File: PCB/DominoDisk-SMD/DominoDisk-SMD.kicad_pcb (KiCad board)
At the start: 2 copper layers, 45.7 x 38.9 mm, 32 parts, among them J1 Daisy port out, J2 ICSP_ISP6, J3 UART, J4 Daisy port in, K1 HYC77-TF09-200, U1 PC817C-S, U2 ATmega328P-AU, U3 SE5218, U4 TXB0104QPWRQ1, Y1 Crystal_GND2

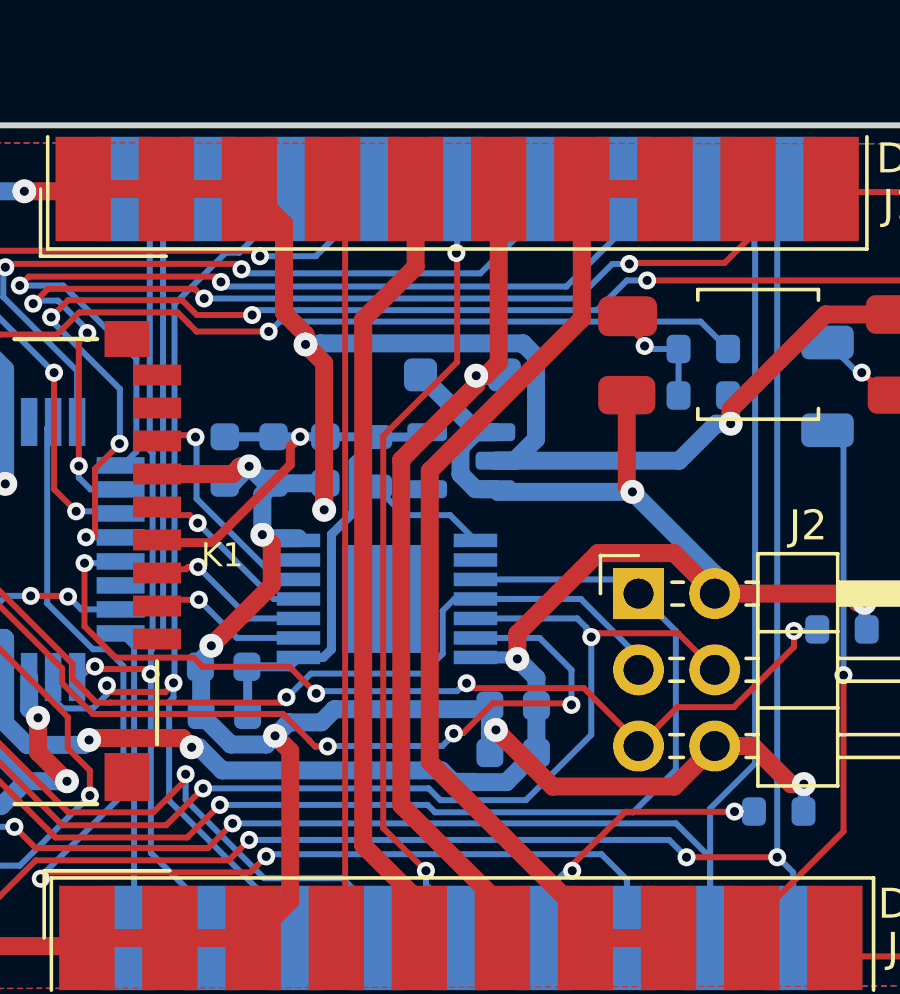
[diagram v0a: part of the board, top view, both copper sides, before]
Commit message: Fix part number on Small version
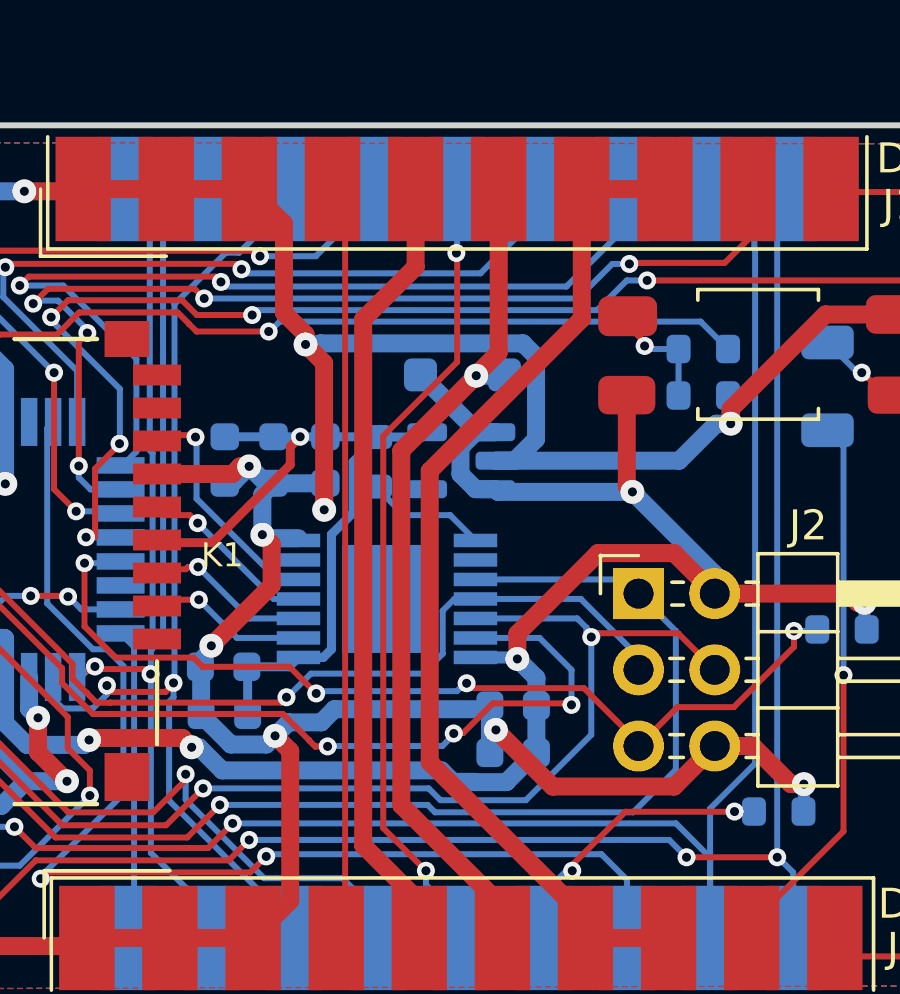
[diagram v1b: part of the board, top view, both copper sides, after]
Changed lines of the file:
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@@
 	)
 	(segment
-		(start 123.4066 50.415504)
+		(start 123.4066 50.0754)
 		(end 123.4066 44.6278)
+		(width 0.6)
+		(layer "F.Cu")
+		(net 22)
+	)
+	(segment
+		(start 122.6566 50.8254)
+		(end 123.4066 50.0754)
 		(width 0.6)
 		(layer "F.Cu")
@@
 	)
 	(segment
-		(start 122.6566 50.8508)
-		(end 122.6566 51.1556)
-		(width 0.6)
-		(layer "F.Cu")
-		(net 22)
-	)
-	(segment
-		(start 120.1588 53.6534)
+		(start 120.1588 53.3486)
 		(end 120.1588 65.1678)
 		(width 0.6)
@@
 	)
 	(segment
-		(start 122.6566 51.1556)
-		(end 120.1588 53.6534)
+		(start 122.6566 50.8508)
+		(end 120.1588 53.3486)
 		(width 0.6)
 		(layer "F.Cu")
@@
 	(segment
 		(start 122.6566 50.8508)
-		(end 122.971304 50.8508)
+		(end 122.6566 50.8254)
 		(width 0.6)
 		(layer "F.Cu")
-		(net 22)
-	)
-	(segment
-		(start 122.971304 50.8508)
-		(end 123.4066 50.415504)
-		(width 0.6)
-		(layer "F.Cu")

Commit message: Same on Domino
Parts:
- C2: value 100nF -> 100n
- R4: value 10K -> 10k
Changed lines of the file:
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@@
 			)
 		)
-		(property "Value" "100nF"
+		(property "Value" "100n"
 			(at 0 -1.43 90)
 			(layer "B.Fab")
@@
 			)
 		)
-		(property "LCSC" "C28233"
+		(property "LCSC" " C1590"
 			(at 0 0 270)
 			(unlocked yes)
@@
 			)
 		)
-		(property "Value" "10K"
+		(property "Value" "10k"
 			(at 0 -1.43 0)
 			(layer "B.Fab")
@@
 			)
 		)
-		(property "LCSC" "C17414"
+		(property "LCSC" " C177337"
 			(at 0 0 0)
 			(unlocked yes)

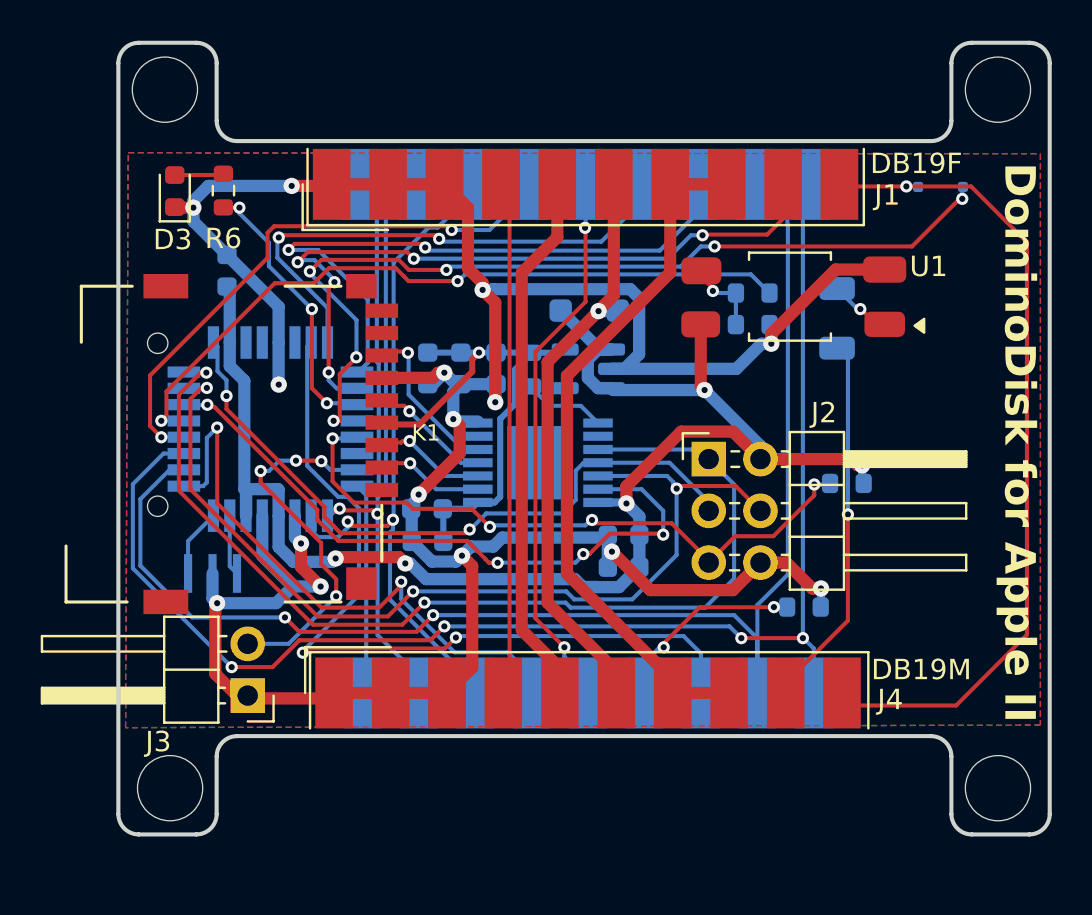
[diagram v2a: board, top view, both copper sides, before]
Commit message: Layout cleanups
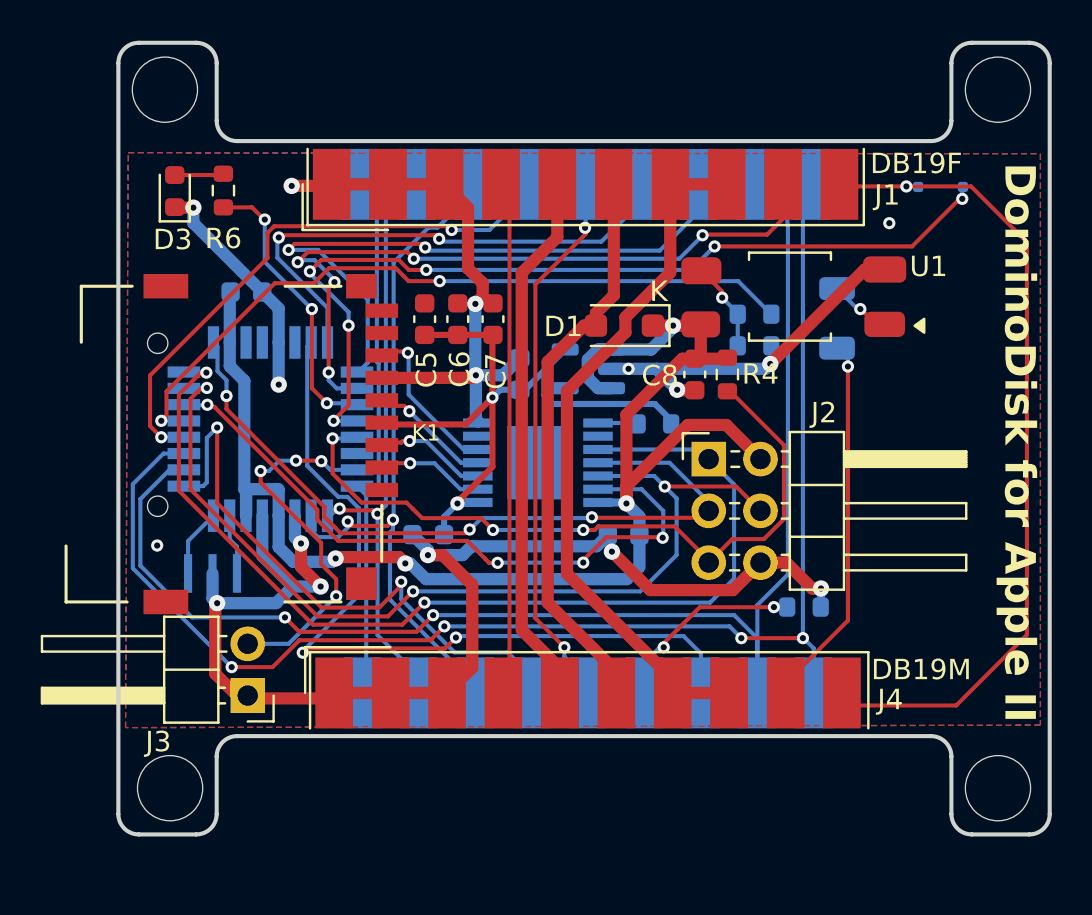
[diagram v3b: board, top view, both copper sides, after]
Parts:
- C5, C6, C7, C8, D1, R4: moved to F.Cu
- moved C8 10.1 mm to (127.4, 54.0), turned to 90 degrees
- moved C4 9.38 mm to (118.8, 53.9), turned to -90 degrees
- moved R4 7.94 mm to (129.0, 54.0), turned to -90 degrees
- moved R7 6.58 mm to (125.4, 56.4), turned to 180 degrees
- moved C5 2.42 mm to (114.1, 51.2), turned to -90 degrees
- moved C6 2.42 mm to (115.7, 51.2), turned to -90 degrees
- moved C7 2.42 mm to (117.5, 51.2), turned to -90 degrees
- moved D1 1.88 mm to (123.9, 51.6), turned to 180 degrees
- moved C2 1.41 mm to (105.4, 49.9), turned to 0 degrees
- moved C10 1.27 mm to (114.3, 61.8)
- moved R3 1.05 mm to (130.3, 51.0)
- moved R2 1.05 mm to (130.3, 52.6)
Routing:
- net GND: track 145.3 -> 118.1 mm, vias 15 -> 16
- net 3V3: track 26.4 -> 32.8 mm, vias 1 -> 2
- net RESET: track 31.3 -> 35.3 mm, vias 4 -> 3
- net SCK: track 33.1 -> 36.7 mm, vias 2 -> 3
- net 5V_burgerDisk: track 75.5 -> 72.4 mm, vias 5 -> 4
- net OE: track 3.96 -> 1.96 mm
- net Net-(R2-Pad2): track 3.65 -> 4.42 mm
- net 5V_apple2: track 27.6 -> 27.0 mm, vias 1 -> 0

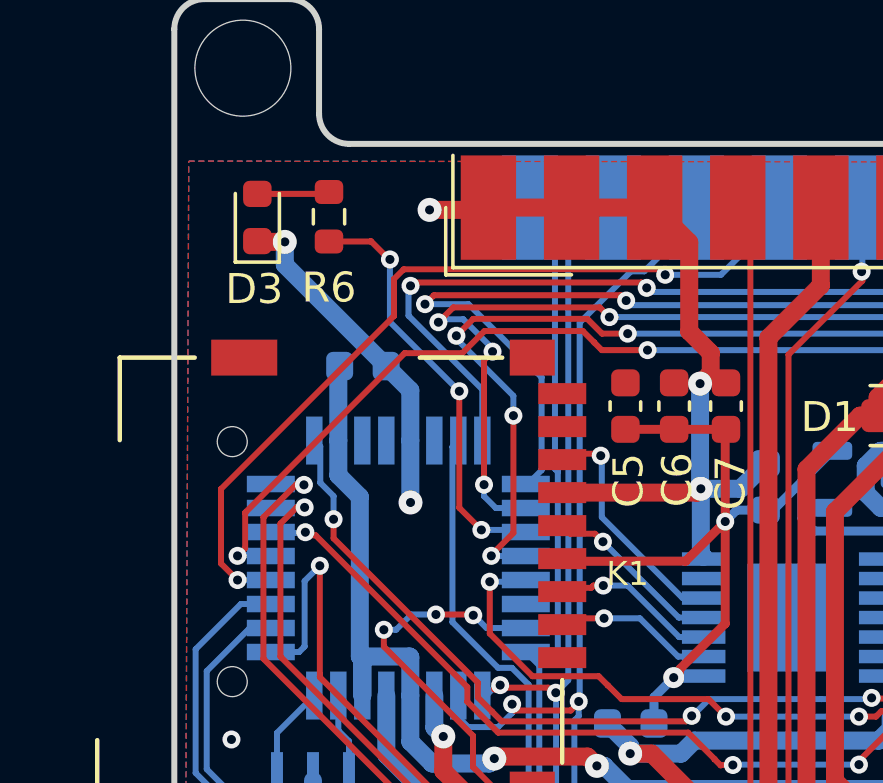
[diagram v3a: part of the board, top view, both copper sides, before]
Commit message: Add libraries and update Domino/Angled
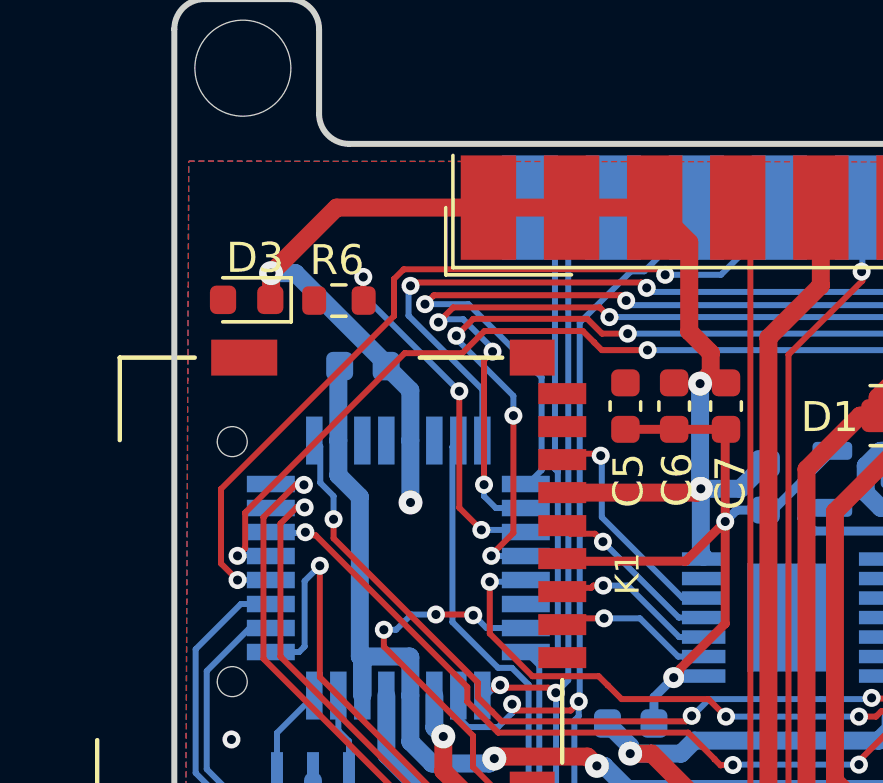
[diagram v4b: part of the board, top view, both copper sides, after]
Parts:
- K1: footprint MICROSD-HYC77-TF09-200:MICROSD-HYC77-TF09-200 -> HYC04-TF09-200:MICROSD-HYC77-TF09-200
- moved R6 2.81 mm to (104.6, 47.7), turned to 0 degrees
- moved D3 2.77 mm to (101.5, 47.7), turned to 180 degrees
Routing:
- net GND: track 118.1 -> 124.0 mm, vias 16 -> 15
- net Net-(D3-A): track 2.12 -> 0.00 mm
- net LED: track 14.0 -> 12.3 mm

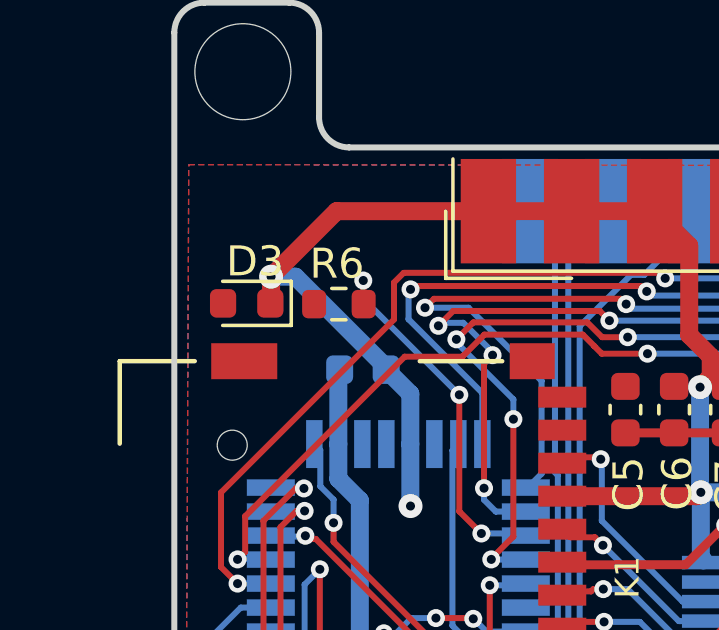
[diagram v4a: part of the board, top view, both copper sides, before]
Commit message: Add logo (thanks to Javier Rivera!!)
Add my own micro/SD modules
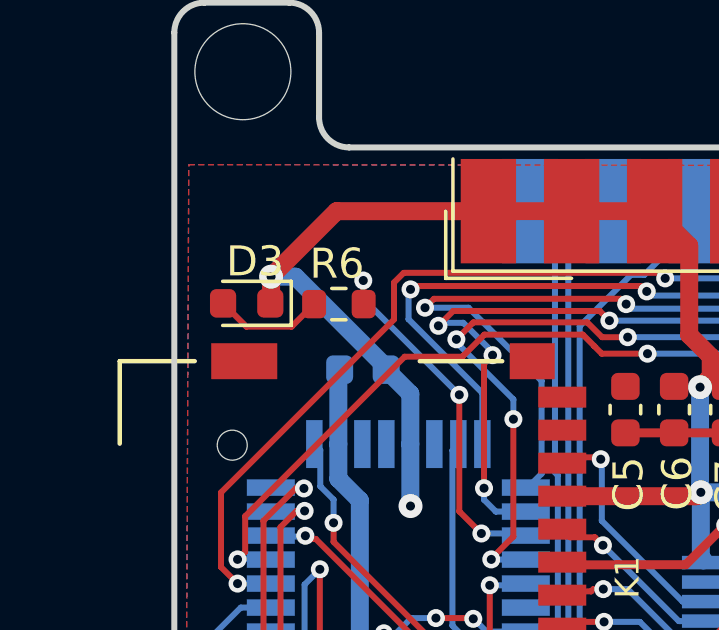
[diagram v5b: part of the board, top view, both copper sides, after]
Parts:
- added G***: LOGO, LOGO, B.Cu at (138.1, 60.0)
- U4: value TXB0104QPWRQ1 -> TXB0104PWR
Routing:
- net Net-(D3-A): track 0.00 -> 3.67 mm

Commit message: Cleanups
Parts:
- C8: moved to B.Cu
- moved C2 13.5 mm to (107.3, 63.3), turned to 180 degrees
- moved R7 6.63 mm to (119.4, 53.7), turned to -90 degrees
- moved C7 4.06 mm to (117.0, 55.3)
- moved C5 4.05 mm to (114.0, 55.3)
- moved C6 4.05 mm to (115.5, 55.3)
- moved D3 2.17 mm to (103.7, 47.9), turned to 90 degrees
- moved C8 2.04 mm to (125.3, 53.7)
- moved C4 0.98 mm to (117.9, 53.7)
- moved R6 0.81 mm to (105.4, 47.9), turned to 90 degrees
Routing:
- net 3V3: track 32.8 -> 21.2 mm, vias 2 -> 1
- net CS: track 32.9 -> 38.8 mm
- net SCK: track 36.7 -> 42.0 mm
- net TX: track 18.1 -> 13.0 mm, vias 4 -> 2
- net PH3_in: track 28.4 -> 23.6 mm
- net 5V_burgerDisk: track 72.4 -> 68.6 mm, vias 4 -> 5
- net OE: track 1.96 -> 4.05 mm
- net Net-(D3-A): track 3.67 -> 2.31 mm
- net MOSI: track 46.6 -> 47.7 mm
- net SCLK_L: track 5.98 -> 6.97 mm
- net MISO: track 50.1 -> 51.0 mm
- net LED: track 12.3 -> 11.4 mm
- net PH2: track 33.5 -> 34.2 mm
- net MISO_L: track 7.90 -> 8.58 mm
- net DRV1_in: track 39.9 -> 40.6 mm, vias 2 -> 4
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
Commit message: Fix LED and R6
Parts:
- R6: value 150 -> 100
- Y1: value Crystal_GND2 -> Resonator
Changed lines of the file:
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@@
 			)
 		)
-		(property "Description" ""
+		(property "Description" "Blue LED, 20mA 3.3V"
 			(at 0 0 90)
 			(layer "F.Fab")
@@
 			)
 		)
-		(property "LCSC" "C2288"
+		(property "LCSC" "C965807"
 			(at 0 0 90)
 			(unlocked yes)
@@
 			)
 		)
-		(property "Value" "150"
+		(property "Value" "100"
 			(at 0 1.43 90)
 			(layer "F.Fab")
@@
 			)
 		)
-		(property "LCSC" "C177290"
+		(property "LCSC" "C22369795"
 			(at 0 0 90)
 			(unlocked yes)
@@
 			)
 		)
-		(property "Value" "Crystal_GND2"
+		(property "Value" "Resonator"
 			(at 0 -1.8 0)
 			(layer "B.Fab")
@@
 			)
 		)
-		(property "Description" "Three pin crystal, GND on pin 2"
+		(property "Description" "Three pin, GND on pin 2"
 			(at 0 0 0)
 			(layer "B.Fab")
